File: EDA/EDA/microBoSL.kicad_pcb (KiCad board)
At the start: 4 copper layers, 52 x 15 mm, 65 parts, among them J1 Conn_01x04, J2 Conn_01x03, J3 Conn_01x04, J4 Conn_01x04, J5 Conn_01x02, J6 Conn_01x03, J7 Conn_01x03, J8 USB_B_Micro, J9 MOTOR_OUT, Q1 DMP2165UW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

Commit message: adding silkscreen
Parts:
- moved R8 0.63 mm to (117.0, 108.1)
- moved D3 0.57 mm to (117.0, 105.6)
- moved U3 0.23 mm to (120.1, 106.9)
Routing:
- net GND: track 82.5 -> 86.3 mm, vias 48 -> 47
- net SDA: track 18.8 -> 22.6 mm, vias 1 -> 3
- net A3: track 26.1 -> 24.2 mm
- net TLL_RST: track 35.1 -> 33.5 mm
- net USB_V: track 10.8 -> 9.91 mm
- net TTL_3.3V: track 44.3 -> 44.9 mm
- net Net-(C2-Pad2): track 5.14 -> 4.63 mm
- net SCL: track 21.4 -> 21.1 mm, vias 1 -> 2

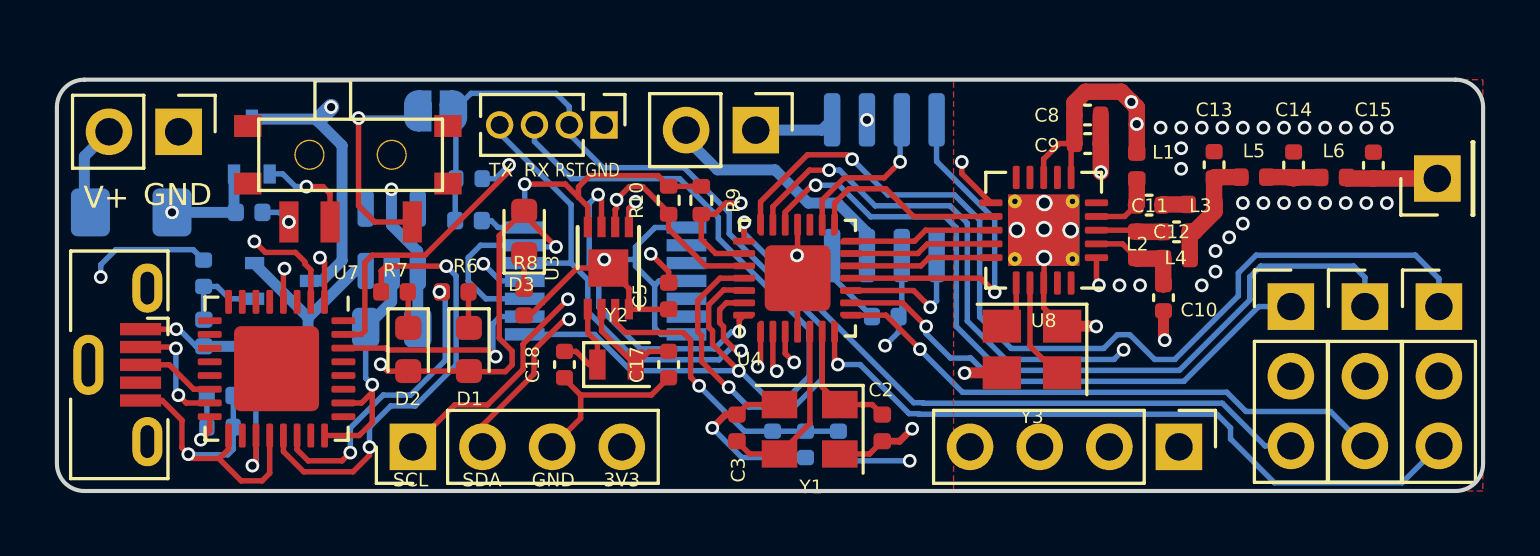
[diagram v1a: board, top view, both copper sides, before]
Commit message: finished layout of pcb
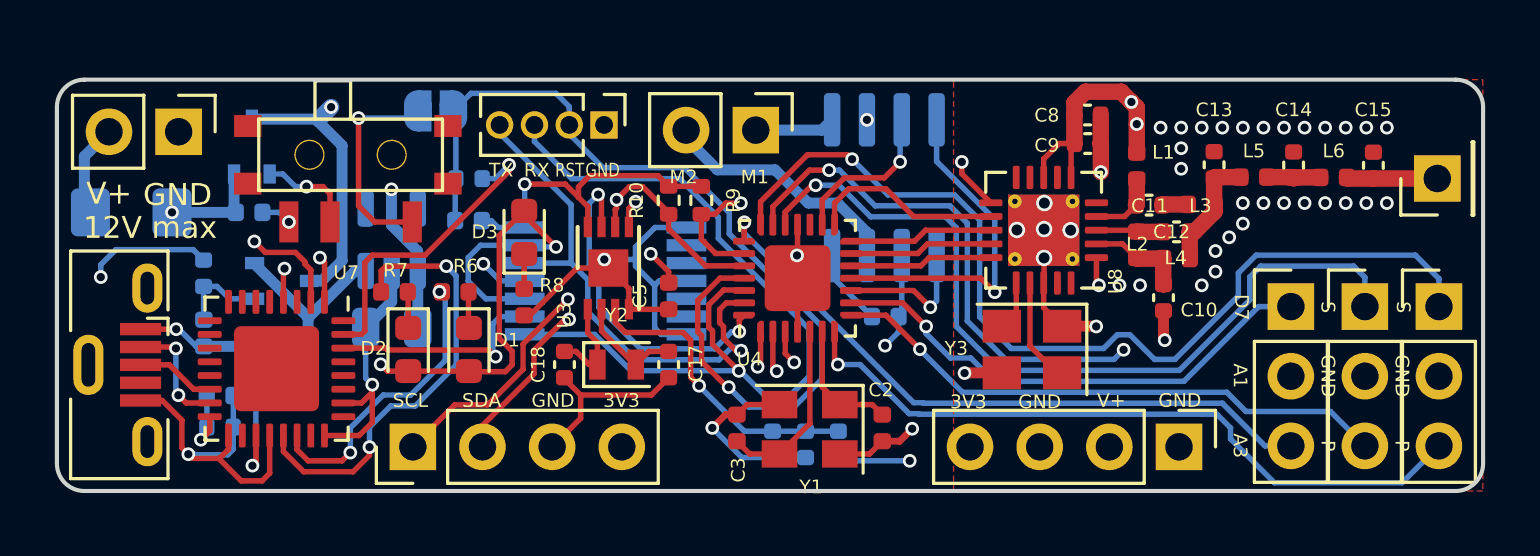
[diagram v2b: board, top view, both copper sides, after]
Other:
- board text added: "12V max"
- board text added: "D7"
- board text added: "M1"
- board text added: "M2"
- board text added: "fuse:1A"
- board text removed: "10"
- board text removed: "11"
- board text removed: "12"
- board text removed: "13"
- board text removed: "3"
- board text removed: "4"
- board text removed: "7"
- board text removed: "8"
- board text removed: "FUSE:1A"
- board text removed: "M-"
